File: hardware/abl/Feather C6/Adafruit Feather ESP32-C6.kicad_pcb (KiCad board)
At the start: 2 copper layers, 50.8 x 22.9 mm, 117 parts, among them Q3 DMG3415U, SW1 KMR2, SW2 KMR2, U1 ESP32-C6-MINI_MINI, U2 AP2112/RT9080-3.3, U3 MCP73831T-2ACI/OT, U4 AHT20-F, U5 AP2112/RT9080-3.3, X1 JSTPH, X2 MAX17048/T, X3 USB C

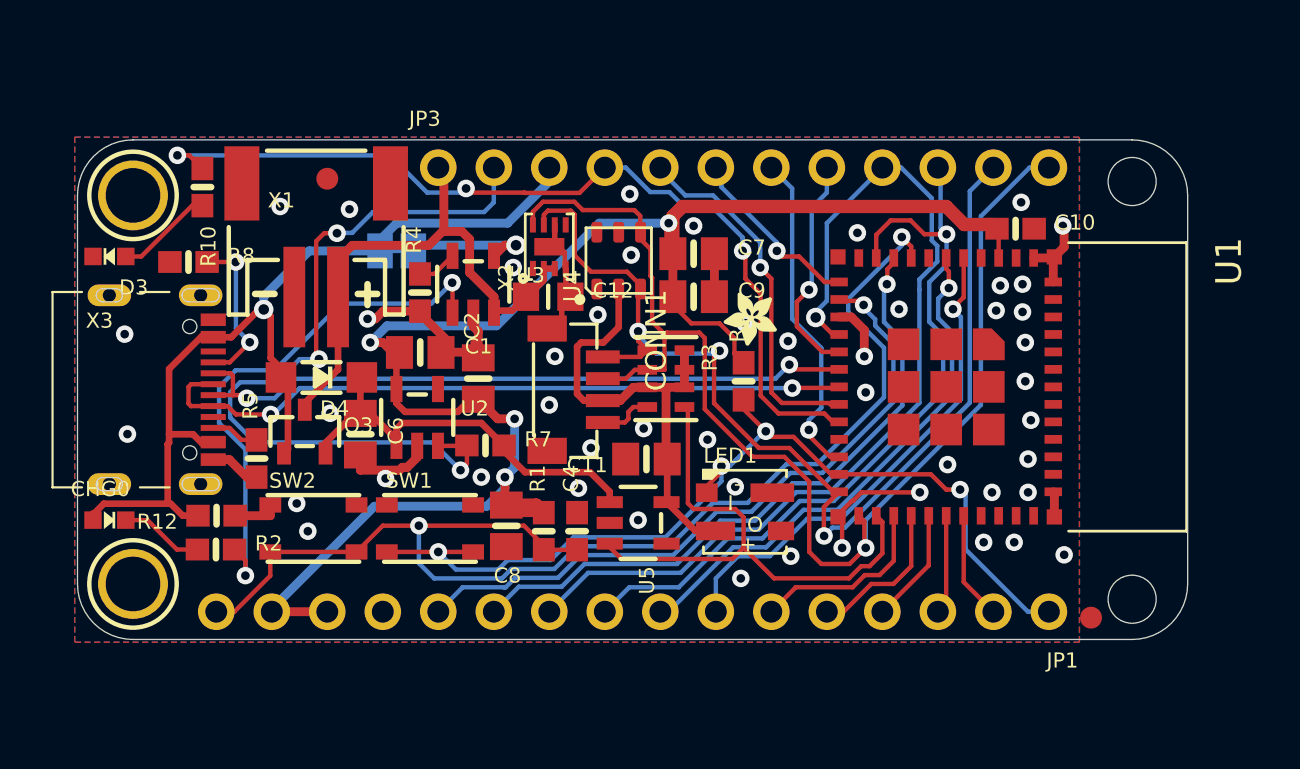
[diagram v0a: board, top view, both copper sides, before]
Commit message: Add ground planes and more ground pins.
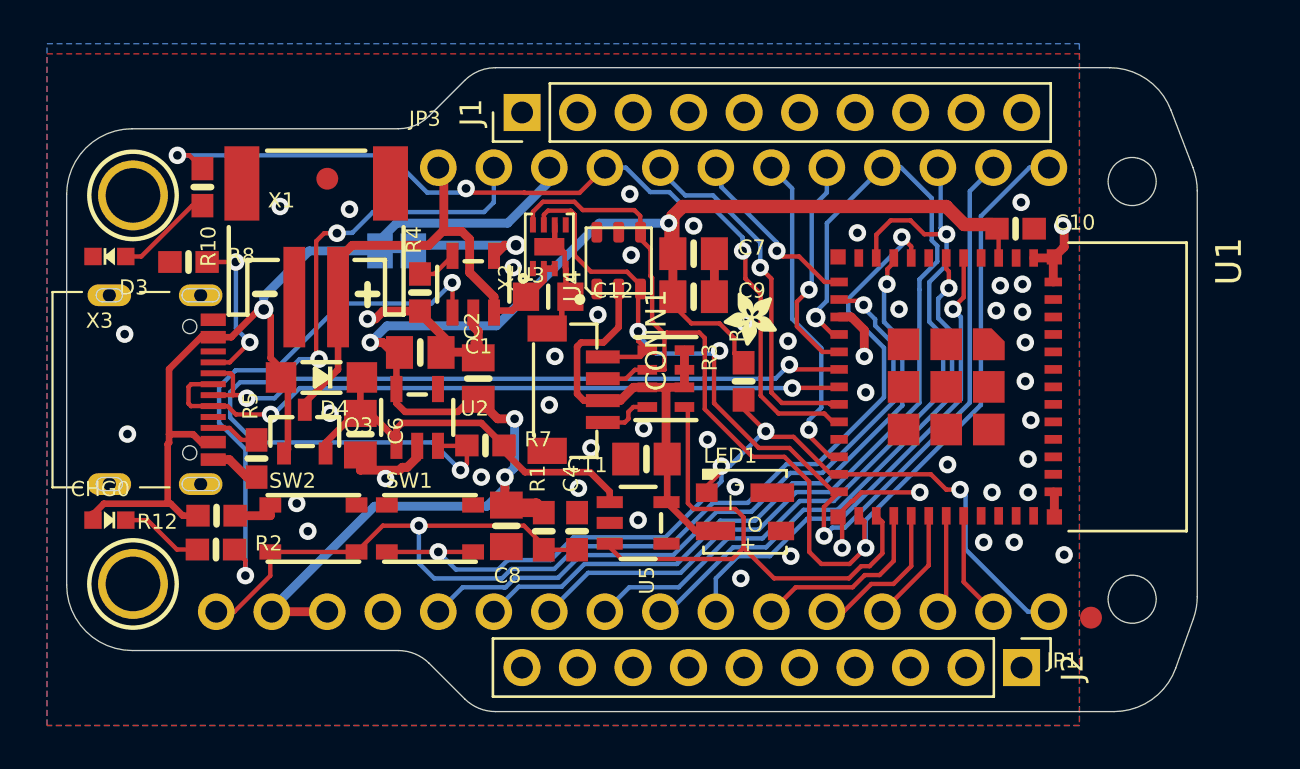
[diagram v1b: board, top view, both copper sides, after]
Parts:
- added J1: Conn_01x10_Pin, Connector_PinHeader_2.54mm:PinHeader_1x10_P2.54mm_Vertical, F.Cu at (143.4, 92.3)
- added J2: Conn_01x10_Pin, Connector_PinHeader_2.54mm:PinHeader_1x10_P2.54mm_Vertical, F.Cu at (166.3, 117.7)
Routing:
- added copper zone on In1.Cu, net GND
- added copper zone on In2.Cu, net GND
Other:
- board size 50.8 x 22.9 mm -> 51.7 x 29.5 mm
- copper layers 2 -> 4

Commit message: Add Adafruit Feather ESP32-C6 version 1.1, originally made on 2025-01-05.
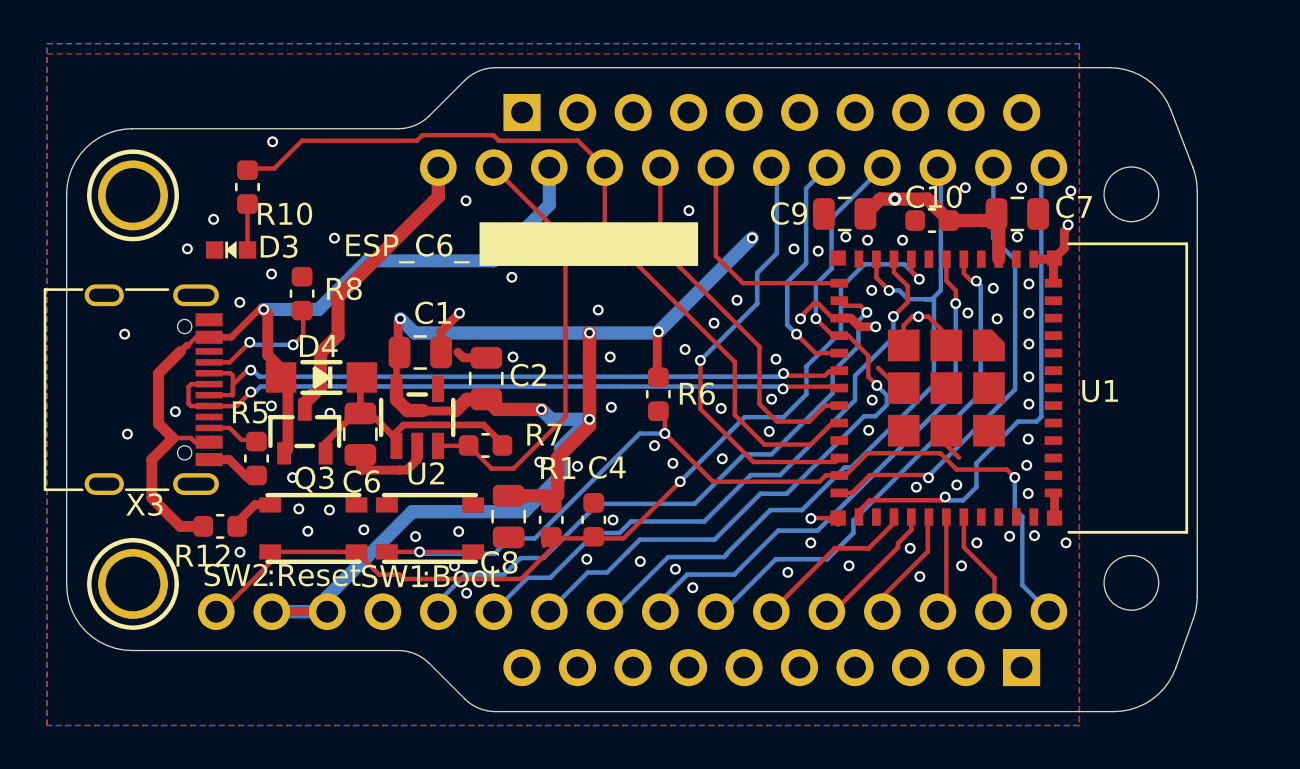
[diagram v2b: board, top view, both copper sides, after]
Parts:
- removed @HOLE0, @HOLE1: , 
- removed C11: 10uF, Adafruit Feather ESP32-C6:0805-NO
- removed C12: 10uF, Adafruit Feather ESP32-C6:_0805MP
- removed CHG0: ORANGE, Adafruit Feather ESP32-C6:CHIPLED_0603_NOOUTLINE
- removed CONN1: JST SH, Adafruit Feather ESP32-C6:JST_SH4_RA
- removed LED1: WS2812B_3535FULL, Adafruit Feather ESP32-C6:LED3535_FULLPADS
- removed PLABEL0: , Adafruit Feather ESP32-C6:PLABEL0
- removed PLABEL1: , Adafruit Feather ESP32-C6:PLABEL1
- removed PLABEL10: , Adafruit Feather ESP32-C6:PLABEL10
- removed PLABEL11: , Adafruit Feather ESP32-C6:PLABEL11
- removed PLABEL12: , Adafruit Feather ESP32-C6:PLABEL12
- removed PLABEL13: , Adafruit Feather ESP32-C6:PLABEL13
- removed PLABEL14: , Adafruit Feather ESP32-C6:PLABEL14
- removed PLABEL15: , Adafruit Feather ESP32-C6:PLABEL15
- removed PLABEL16: , Adafruit Feather ESP32-C6:PLABEL16
- removed PLABEL17: , Adafruit Feather ESP32-C6:PLABEL17
- removed PLABEL18: , Adafruit Feather ESP32-C6:PLABEL18
- removed PLABEL19: , Adafruit Feather ESP32-C6:PLABEL19
- removed PLABEL2: , Adafruit Feather ESP32-C6:PLABEL2
- removed PLABEL20: , Adafruit Feather ESP32-C6:PLABEL20
- removed PLABEL21: , Adafruit Feather ESP32-C6:PLABEL21
- removed PLABEL22: , Adafruit Feather ESP32-C6:PLABEL22
- removed PLABEL23: , Adafruit Feather ESP32-C6:PLABEL23
- removed PLABEL24: , Adafruit Feather ESP32-C6:PLABEL24
- removed PLABEL25: , Adafruit Feather ESP32-C6:PLABEL25
- removed PLABEL26: , Adafruit Feather ESP32-C6:PLABEL26
- removed PLABEL27: , Adafruit Feather ESP32-C6:PLABEL27
- removed PLABEL28: , Adafruit Feather ESP32-C6:PLABEL28
- removed PLABEL29: , Adafruit Feather ESP32-C6:PLABEL29
- removed PLABEL30: , Adafruit Feather ESP32-C6:PLABEL30
- removed PLABEL31: , Adafruit Feather ESP32-C6:PLABEL31
- removed PLABEL32: , Adafruit Feather ESP32-C6:PLABEL32
- removed PLABEL33: , Adafruit Feather ESP32-C6:PLABEL33
- removed PLABEL34: , Adafruit Feather ESP32-C6:PLABEL34
- removed PLABEL35: , Adafruit Feather ESP32-C6:PLABEL35
- removed PLABEL36: , Adafruit Feather ESP32-C6:PLABEL36
- removed PLABEL37: , Adafruit Feather ESP32-C6:PLABEL37
- removed PLABEL38: , Adafruit Feather ESP32-C6:PLABEL38
- removed PLABEL39: , Adafruit Feather ESP32-C6:PLABEL39
- removed PLABEL4: , Adafruit Feather ESP32-C6:PLABEL4
- removed PLABEL40: , Adafruit Feather ESP32-C6:PLABEL40
- removed PLABEL41: , Adafruit Feather ESP32-C6:PLABEL41
- removed PLABEL42: , Adafruit Feather ESP32-C6:PLABEL42
- removed PLABEL43: , Adafruit Feather ESP32-C6:PLABEL43
- removed PLABEL44: , Adafruit Feather ESP32-C6:PLABEL44
- removed PLABEL45: , Adafruit Feather ESP32-C6:PLABEL45
- removed PLABEL46: , Adafruit Feather ESP32-C6:PLABEL46
- removed PLABEL47: , Adafruit Feather ESP32-C6:PLABEL47
- removed PLABEL48: , Adafruit Feather ESP32-C6:PLABEL48
- removed PLABEL49: , Adafruit Feather ESP32-C6:PLABEL49
- removed PLABEL5: , Adafruit Feather ESP32-C6:PLABEL5
- removed PLABEL51: , Adafruit Feather ESP32-C6:PLABEL51
- removed PLABEL52: , Adafruit Feather ESP32-C6:PLABEL52
- removed PLABEL53: , Adafruit Feather ESP32-C6:PLABEL53
- removed PLABEL54: , Adafruit Feather ESP32-C6:PLABEL54
- removed PLABEL55: , Adafruit Feather ESP32-C6:PLABEL55
- removed PLABEL56: , Adafruit Feather ESP32-C6:PLABEL56
- removed PLABEL57: , Adafruit Feather ESP32-C6:PLABEL57
- removed PLABEL58: , Adafruit Feather ESP32-C6:PLABEL58
- removed PLABEL59: , Adafruit Feather ESP32-C6:PLABEL59
- removed PLABEL6: , Adafruit Feather ESP32-C6:PLABEL6
- removed PLABEL60: , Adafruit Feather ESP32-C6:PLABEL60
- removed PLABEL61: , Adafruit Feather ESP32-C6:PLABEL61
- removed PLABEL62: , Adafruit Feather ESP32-C6:PLABEL62
- removed PLABEL63: , Adafruit Feather ESP32-C6:PLABEL63
- removed PLABEL64: , Adafruit Feather ESP32-C6:PLABEL64
- removed PLABEL65: , Adafruit Feather ESP32-C6:PLABEL65
- removed PLABEL66: , Adafruit Feather ESP32-C6:PLABEL66
- removed PLABEL67: , Adafruit Feather ESP32-C6:PLABEL67
- removed PLABEL68: , Adafruit Feather ESP32-C6:PLABEL68
- removed PLABEL7: , Adafruit Feather ESP32-C6:PLABEL7
- removed PLABEL8: , Adafruit Feather ESP32-C6:PLABEL8
- removed PLABEL9: , Adafruit Feather ESP32-C6:PLABEL9
- removed R2, R4: 5.1K, Adafruit Feather ESP32-C6:0603-NO
- removed R3: 10K, Adafruit Feather ESP32-C6:RESPACK_4X0603
- removed SJ1: SOLDERJUMPERCLOSED, Adafruit Feather ESP32-C6:SOLDERJUMPER_CLOSEDWIRE
- removed U$14: , Adafruit Feather ESP32-C6:PCBFEAT-REV-040
- removed U$15: , Adafruit Feather ESP32-C6:FEATHERLOGO_MED
- removed U$26: , Adafruit Feather ESP32-C6:ADAFRUIT_2.5MM
- removed U$34, U$35: FIDUCIAL_1MM, Adafruit Feather ESP32-C6:FIDUCIAL_1MM
- removed U$48: , Adafruit Feather ESP32-C6:ADAFRUIT_5MM
- removed U$53: , Adafruit Feather ESP32-C6:STEMMAQT
- removed U3: MCP73831T-2ACI/OT, Adafruit Feather ESP32-C6:SOT23-5
- removed U4: AHT20-F, Adafruit Feather ESP32-C6:LONGAN-IC_SNR6-1.0-3X3X1MM
- removed U5: AP2112/RT9080-3.3, Adafruit Feather ESP32-C6:SOT23-5
- removed X1: JSTPH, Adafruit Feather ESP32-C6:JSTPH2_BATT
- removed X2: MAX17048/T, Adafruit Feather ESP32-C6:TDFN8_2X2MM
- added G***: LOGO, LOGO, B.Cu at (136.8, 107.1)
- added REF**: OSHW-Logo_5.7x6mm_SilkScreen, Symbol:OSHW-Logo_5.7x6mm_SilkScreen, B.Cu at (134.9, 98.8)
- added U$1: MOUNTINGHOLE2.5, MountingHole:MountingHole_2.5mm, F.Cu at (171.3, 96.1)
- added U$2: MOUNTINGHOLE2.5, MountingHole:MountingHole_2.5mm, F.Cu at (171.3, 113.8)
- C1, C2, C6, C7, C8, C9: footprint Adafruit Feather ESP32-C6:0805-NO -> Capacitor_SMD:C_0805_2012Metric
- C10, C4, R1, R10, R12, R5, R6, R7, R8: footprint Adafruit Feather ESP32-C6:0603-NO -> Capacitor_SMD:C_0603_1608Metric
- J1, J2, JP1, JP3: moved to B.Cu
- X3: footprint Adafruit Feather ESP32-C6:USB_C_CUSB31-CFM2AX-01-X -> Connector_USB:USB_C_Receptacle_G-Switch_GT-USB-7010ASV
- moved C7 14.9 mm to (166.1, 97.0)
- moved C9 7.88 mm to (158.2, 97.0), turned to 180 degrees
- moved D3 5.58 mm to (130.1, 98.6)
- moved R8 5.40 mm to (133.4, 100.6), turned to -90 degrees
- moved R6 3.95 mm to (149.7, 105.2)
- moved C10 3.84 mm to (162.2, 97.3), turned to 180 degrees
- moved R10 2.06 mm to (130.9, 95.7)
- moved X3 1.64 mm to (125.4, 105.0)
- moved C4 0.92 mm to (146.7, 111.0)
- moved R1 0.62 mm to (144.8, 111.0)
- moved R12 0.52 mm to (129.6, 111.3)
- moved C8 0.44 mm to (142.8, 110.8)
- moved C2 0.37 mm to (141.8, 104.5)
- moved U1 0.05 mm to (162.9, 104.9)
- turned J1 to -90 degrees
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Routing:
- net /SDA: track 57.3 -> 23.0 mm
- net /SCL: track 49.7 -> 21.1 mm, vias 3 -> 1
- net /I2C_PWR: track 24.6 -> 0.00 mm
- net Net-(U3-STAT): track 24.6 -> 0.00 mm, vias 2 -> 0
- net /VSENSOR: track 21.4 -> 0.00 mm
- net /EN: track 35.9 -> 20.0 mm, vias 3 -> 0
- net GND: track 42.7 -> 30.6 mm, vias 49 -> 86
- net /RESET: track 56.3 -> 44.4 mm
- net VBAT: track 25.1 -> 13.6 mm
- net /A2/IO6: track 43.1 -> 33.5 mm, vias 1 -> 2
- net 3.3V: track 77.1 -> 84.0 mm, vias 4 -> 7
- net /VHI: track 19.3 -> 12.8 mm
- net Net-(U3-VDD): track 6.01 -> 0.00 mm, vias 1 -> 0
- net /IO8: track 15.2 -> 20.3 mm
- net /IO15: track 41.6 -> 37.1 mm, vias 3 -> 0
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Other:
- board text added: "10xGND"
- board text added: "3.3V"
- board text added: ":Boot"
- board text added: ":Reset"
- board text added: "A0"
- board text added: "A1"
- board text added: "A4"
- board text added: "A5"
- board text added: "EN"
- board text added: "ESP32-C6 Feather"
- board text added: "ESP_C6_"
- board text added: "GND"
- board text added: "Io0"
- board text added: "Io14"
- board text added: "Io15"
- board text added: "Io5"
- board text added: "Io6"
- board text added: "Io7"
- board text added: "Io8"
- board text added: "Io9"
- board text added: "Lampe"
- board text added: "MISO"
- board text added: "MOSI"
- board text added: "RESET"
- board text added: "RX"
- board text added: "SCK"
- board text added: "SCL"
- board text added: "SDA"
- board text added: "TX"
- board text added: "VBAT"
- board text added: "VBUS"
- board text added: "https://beste-lampe.de Based on ESP32-C6 Feather STEMMA QT by Adafruit CC BY-SA 3.0"
- board text added: "v1.1"
